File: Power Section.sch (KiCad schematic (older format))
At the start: 21 parts, among them J1 BATT, J17 CK-JS102011SAQN, Q1 IRLML9301TRPBF, Q7 IRLML9301TRPBF, U1 LM1117LDX, U2 LM1117LDX

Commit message: Holy $hi3t
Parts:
- added J10, J5, J9: BATT, Connector_PinHeader_2.54mm:PinHeader_1x02_P2.54mm_Vertical, symbol Connector_Generic:Conn_01x02
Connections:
- net BATT+: now also J9.1 (Pin_1)
- net GND: now also J10.2 (Pin_2), J5.2 (Pin_2); no longer J1.2 (Pin_2)
- new net: J1.2 (Pin_2), J10.1 (Pin_1), J5.1 (Pin_1), J9.2 (Pin_2)
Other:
- moved on the sheet: J1
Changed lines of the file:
@@
 L Connector_Generic:Conn_01x02 J1
 U 1 1 5E80D37A
-P 1550 2700
-F 0 "J1" H 1468 2917 50  0000 C CNN
-F 1 "BATT" H 1468 2826 50  0000 C CNN
-F 2 "Connector_PinHeader_2.54mm:PinHeader_1x02_P2.54mm_Vertical" H 1550 2700 50  0001 C CNN
-F 3 "~" H 1550 2700 50  0001 C CNN
-	1    1550 2700
+P 1250 2700
+F 0 "J1" H 1168 2917 50  0000 C CNN
+F 1 "BATT" H 1168 2826 50  0000 C CNN
+F 2 "Connector_PinHeader_2.54mm:PinHeader_1x02_P2.54mm_Vertical" H 1250 2700 50  0001 C CNN
+F 3 "~" H 1250 2700 50  0001 C CNN
+	1    1250 2700
 	-1   0    0    -1
 $EndComp
-Wire Wire Line
-	1750 2800 1900 2800
 Wire Wire Line
 	3800 2900 4200 2900
@@
 L power:GND #PWR0195
 U 1 1 5E892532
-P 1900 3550
-F 0 "#PWR0195" H 1900 3300 50  0001 C CNN
-F 1 "GND" H 1905 3377 50  0000 C CNN
-F 2 "" H 1900 3550 50  0001 C CNN
-F 3 "" H 1900 3550 50  0001 C CNN
-	1    1900 3550
+P 1800 3550
+F 0 "#PWR0195" H 1800 3300 50  0001 C CNN
+F 1 "GND" H 1805 3377 50  0000 C CNN
+F 2 "" H 1800 3550 50  0001 C CNN
+F 3 "" H 1800 3550 50  0001 C CNN
+	1    1800 3550
 	1    0    0    -1
 $EndComp
@@
 	1    0    0    1
 $EndComp
-Wire Wire Line
-	2100 2700 1750 2700
 $Comp
 L Device:R_Small R51
@@
 $EndComp
 Wire Wire Line
-	1900 2800 1900 3550
-Wire Wire Line
 	3800 3100 3800 3550
-Connection ~ 1900 3550
+Connection ~ 1800 3550
 Wire Wire Line
 	3050 3400 3050 3550
 Wire Wire Line
 	3050 3550 3550 3550
-Wire Wire Line
-	1900 3550 3050 3550
-Connection ~ 3050 3550
 Wire Wire Line
 	3350 2700 3550 2700
@@
 Text Notes 3550 2500 0    50   ~ 0
 1:3 voltage divider
+$Comp
+L Connector_Generic:Conn_01x02 J5
+U 1 1 5F9516BF
+P 1250 3100
+F 0 "J5" H 1168 3317 50  0000 C CNN
+F 1 "BATT" H 1168 3226 50  0000 C CNN
+F 2 "Connector_PinHeader_2.54mm:PinHeader_1x02_P2.54mm_Vertical" H 1250 3100 50  0001 C CNN
+F 3 "~" H 1250 3100 50  0001 C CNN
+	1    1250 3100
+	-1   0    0    -1
+$EndComp
+$Comp
+L Connector_Generic:Conn_01x02 J9
+U 1 1 5F956258
+P 1600 2700
+F 0 "J9" H 1518 2917 50  0000 C CNN
+F 1 "BATT" H 1518 2826 50  0000 C CNN
+F 2 "Connector_PinHeader_2.54mm:PinHeader_1x02_P2.54mm_Vertical" H 1600 2700 50  0001 C CNN
+F 3 "~" H 1600 2700 50  0001 C CNN
+	1    1600 2700
+	-1   0    0    -1
+$EndComp
+$Comp
+L Connector_Generic:Conn_01x02 J10
+U 1 1 5F95794D
+P 1600 3100
+F 0 "J10" H 1518 3317 50  0000 C CNN
+F 1 "BATT" H 1518 3226 50  0000 C CNN
+F 2 "Connector_PinHeader_2.54mm:PinHeader_1x02_P2.54mm_Vertical" H 1600 3100 50  0001 C CNN
+F 3 "~" H 1600 3100 50  0001 C CNN
+	1    1600 3100
+	-1   0    0    -1
+$EndComp
+Wire Wire Line
+	1450 2700 1800 2700
+Connection ~ 1800 2700
+Wire Wire Line
+	1450 2800 1800 2800
+Wire Wire Line
+	1800 2800 1800 3100
+Connection ~ 1800 2800
+Wire Wire Line
+	1450 3100 1800 3100
+Connection ~ 1800 3100
+Wire Wire Line
+	1450 3200 1800 3200
+Connection ~ 1800 3200
+Wire Wire Line
+	1800 3200 1800 3550
+Wire Wire Line
+	1800 2700 2100 2700
+Wire Wire Line
+	1800 3550 3050 3550
+Connection ~ 3050 3550
 $EndSCHEMATC

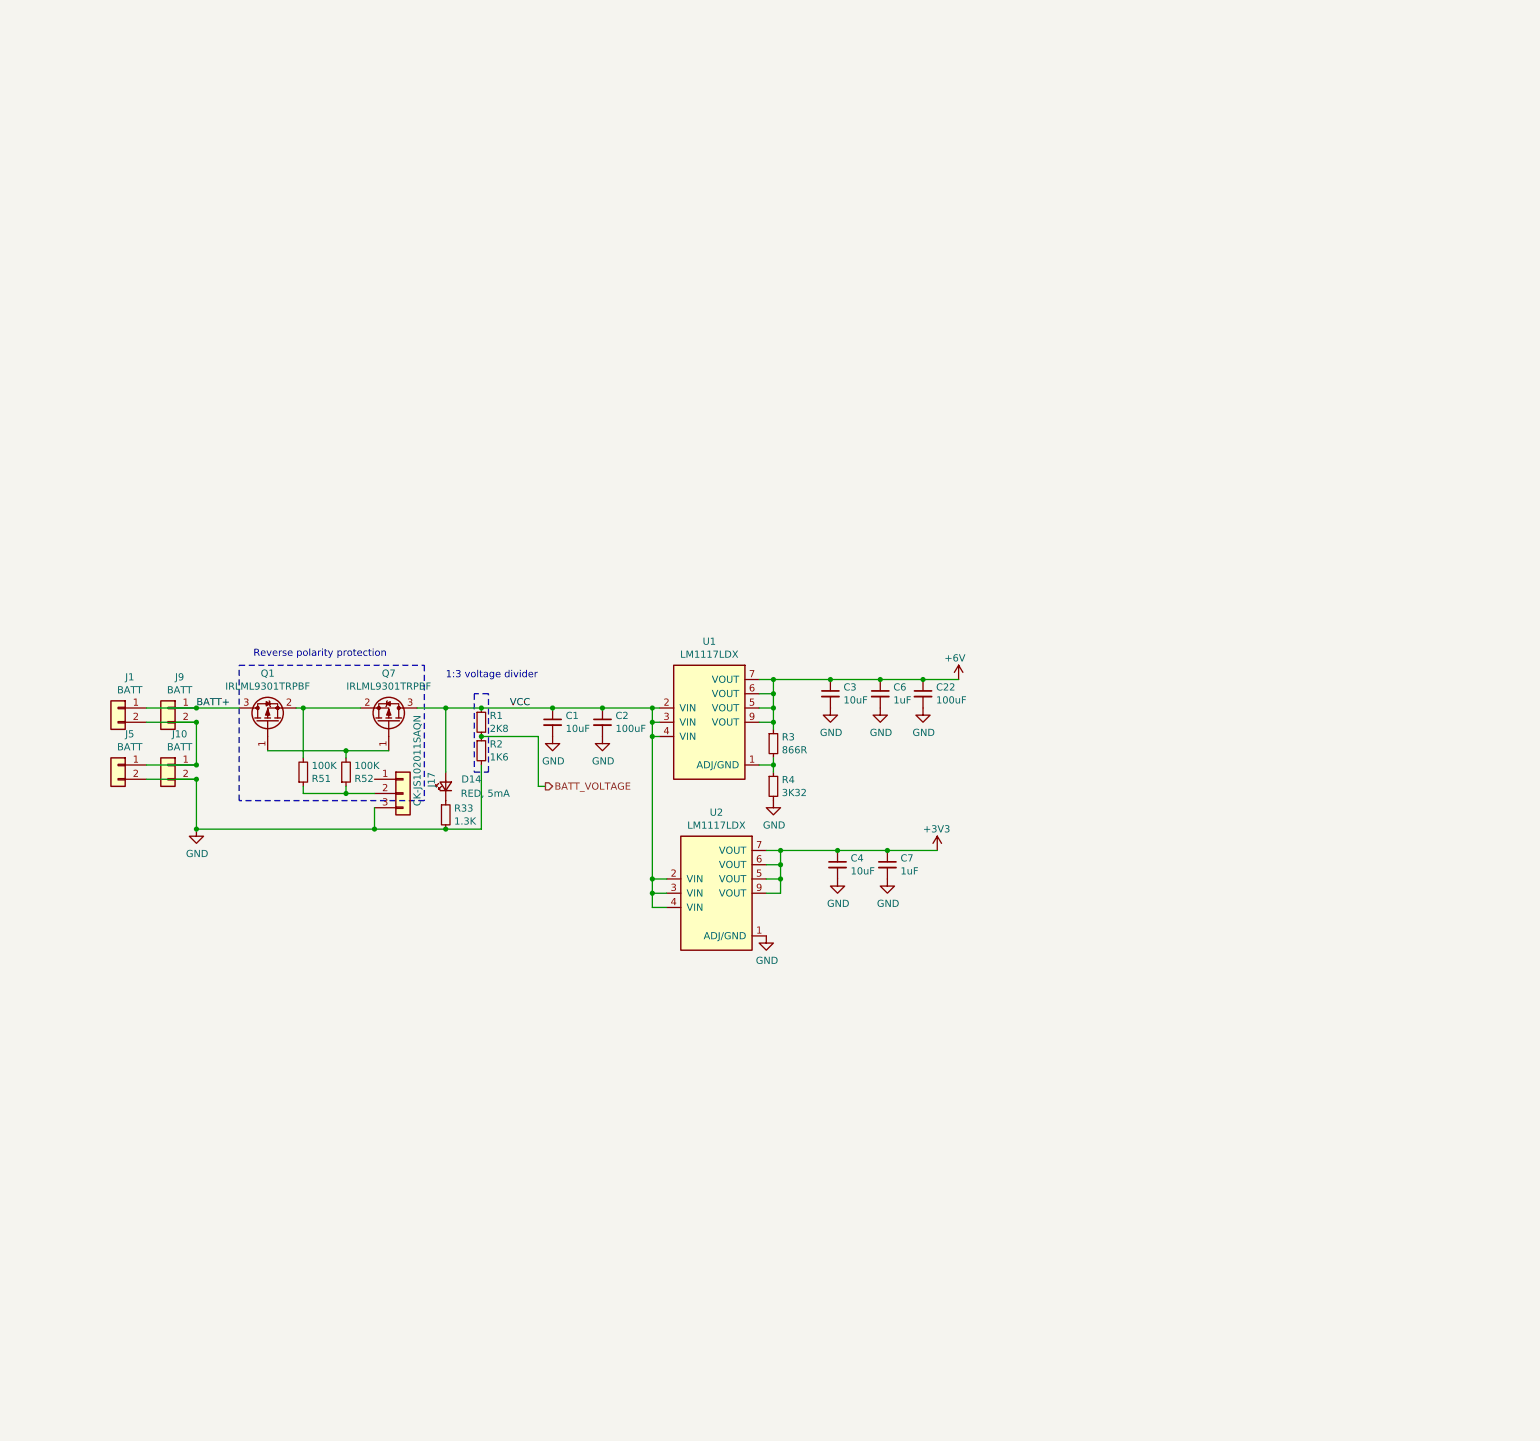
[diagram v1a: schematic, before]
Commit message: USB-C PD charging and cell balancing.
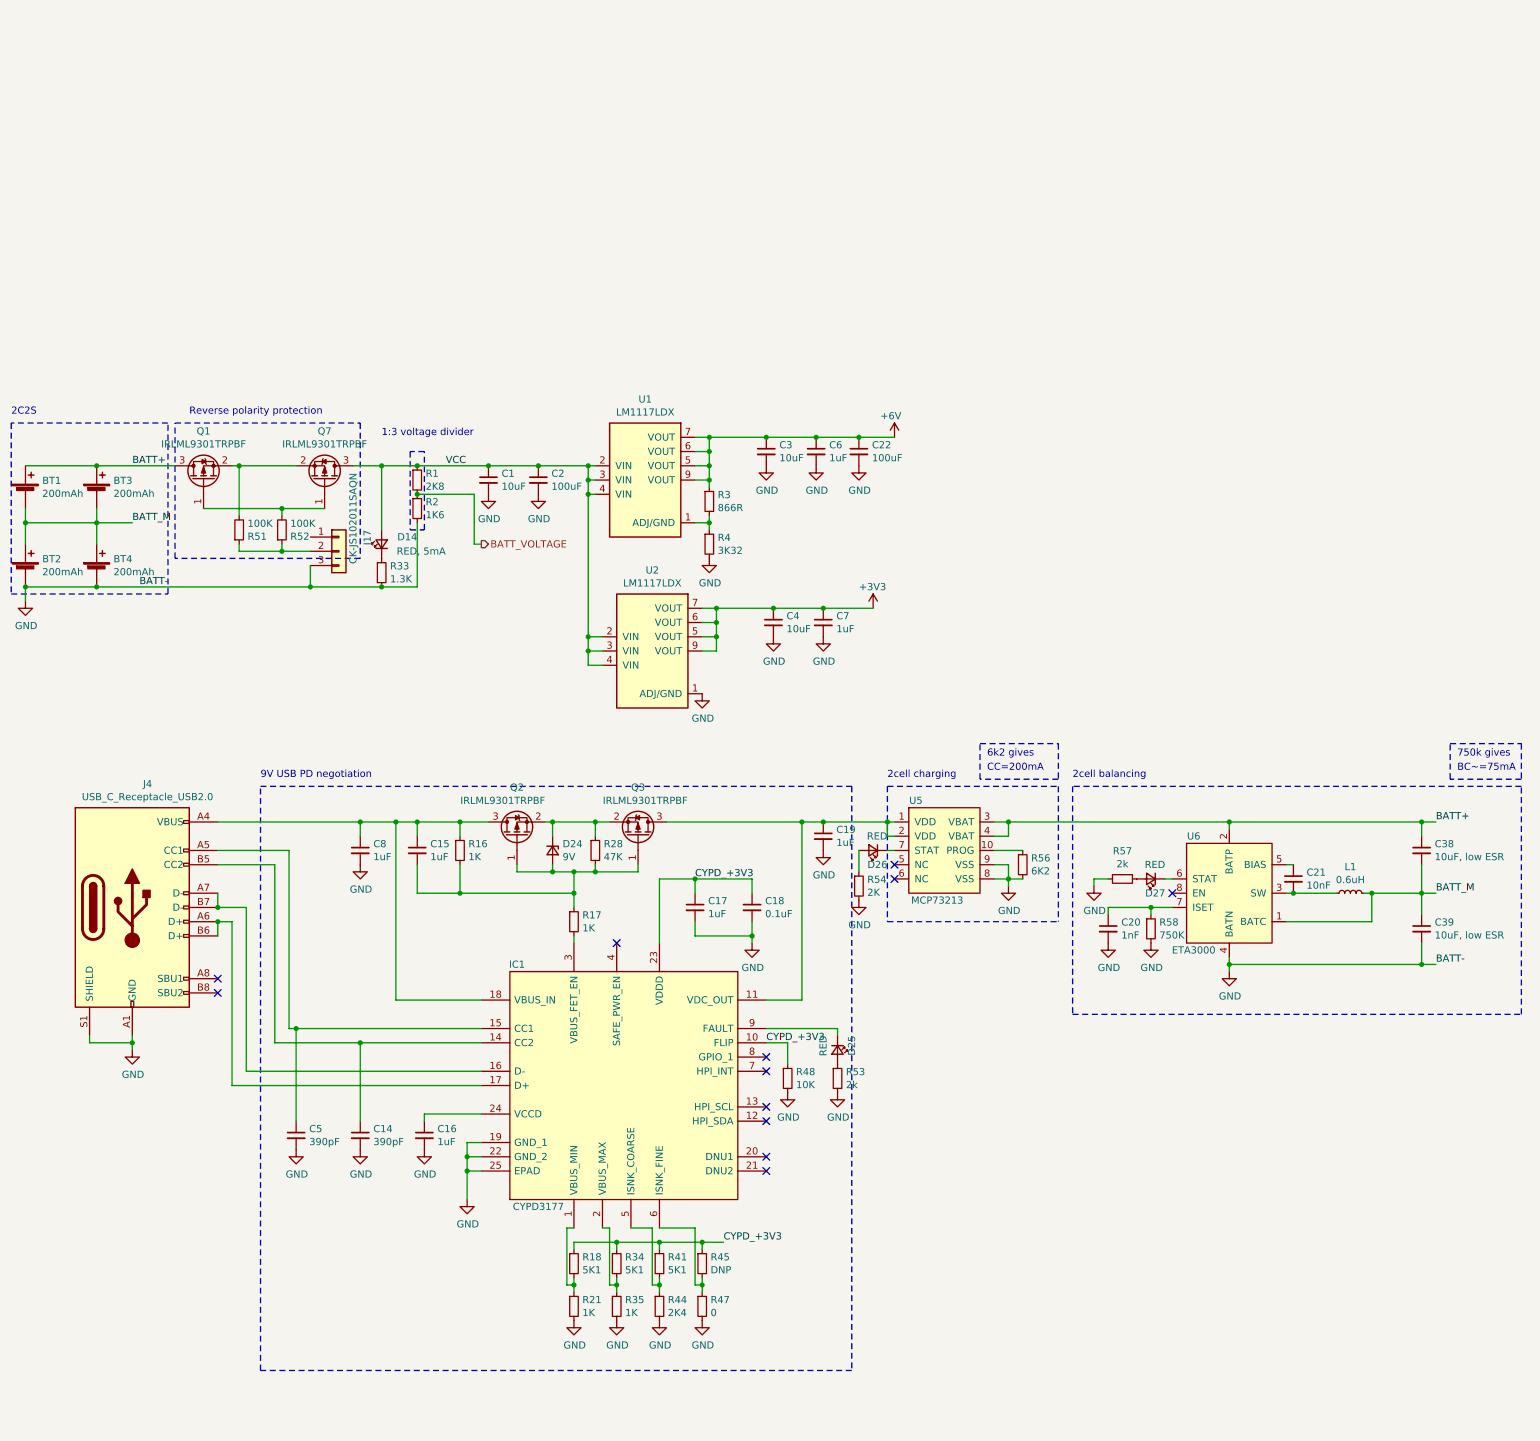
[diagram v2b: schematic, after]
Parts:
- removed J1, J10, J5, J9: BATT, Connector_PinHeader_2.54mm:PinHeader_1x02_P2.54mm_Vertical, symbol Connector_Generic:Conn_01x02
- added BT1, BT2, BT3, BT4: 200mAh, Connector_PinHeader_1.27mm:PinHeader_1x02_P1.27mm_Vertical, symbol Device:Battery_Cell
- added C14, C5: 390pF, Capacitor_SMD:C_0603_1608Metric, symbol Device:C_Small
- added C15, C16, C17, C19, C8: 1uF, Capacitor_SMD:C_0603_1608Metric, symbol Device:C_Small
- added C18: 0.1uF, Capacitor_SMD:C_0603_1608Metric, symbol Device:C_Small
- added C20: 1nF, Capacitor_SMD:C_0603_1608Metric, symbol Device:C_Small
- added C21: 10nF, Capacitor_SMD:C_0603_1608Metric, symbol Device:C_Small
- added C38, C39: 10uF, low ESR, Capacitor_SMD:C_0603_1608Metric, symbol Device:C_Small
- added D24: 9V, Diode_SMD:D_SOD-52, symbol Device:D_Zener_Small
- added D25, D26, D27: RED, LED_SMD:LED_0402_1005Metric, symbol Device:LED_Small
- added IC1: CYPD3177, CYPD3177-24LQXI:QFN50P400X400X60-25N-D, symbol CYPD3177-24LQXI:CYPD3177
- added J4: USB_C_Receptacle_USB2.0, Connector_USB:USB_C_Receptacle_GCT_USB4085, symbol Connector:USB_C_Receptacle_USB2.0
- added L1: 0.6uH, Inductor_SMD:L_0603_1608Metric, symbol Device:L_Small
- added Q2, Q3: IRLML9301TRPBF, Package_TO_SOT_SMD:SOT-23, symbol Device:Q_PMOS_GSD
- added R16, R17, R21, R35: 1K, Resistor_SMD:R_0402_1005Metric, symbol Device:R_Small
- added R18, R34, R41: 5K1, Resistor_SMD:R_0402_1005Metric, symbol Device:R_Small
- added R28: 47K, Resistor_SMD:R_0402_1005Metric, symbol Device:R_Small
- added R44: 2K4, Resistor_SMD:R_0402_1005Metric, symbol Device:R_Small
- added R45: DNP, Resistor_SMD:R_0402_1005Metric, symbol Device:R_Small
- added R47: 0, Resistor_SMD:R_0402_1005Metric, symbol Device:R_Small
- added R48: 10K, Resistor_SMD:R_0402_1005Metric, symbol Device:R_Small
- added R53, R57: 2k, Resistor_SMD:R_0402_1005Metric, symbol Device:R_Small
- added R54: 2K, Resistor_SMD:R_0402_1005Metric, symbol Device:R_Small
- added R56: 6K2, Resistor_SMD:R_0402_1005Metric, symbol Device:R_Small
- added R58: 750K, Resistor_SMD:R_0402_1005Metric, symbol Device:R_Small
- added U5: MCP73213, Package_DFN_QFN:DFN-10-1EP_3x3mm_P0.5mm_EP1.55x2.48mm, symbol synermycha-electronics:MCP73213
- added U6: ETA3000, Package_DFN_QFN:DFN-8-1EP_2x2mm_P0.5mm_EP0.6x1.2mm, symbol synermycha-electronics:ETA3000
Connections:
- net BATT+: now also BT1.1 (+), BT3.1 (+), C38.1, U5.3 (VBAT), U5.4 (VBAT), U6.2 (BATP)
- net GND: now also BT2.2 (-), BT4.2 (-), C14.2, C16.2, C17.2, C18.2, C19.2, C20.2, C39.2, C5.2, C8.2, IC1.19 (GND_1), IC1.22 (GND_2), IC1.25 (EPAD), J4.A1 (GND), J4.A12 (GND), J4.B1 (GND), J4.B12 (GND), J4.S1 (SHIELD), R21.2, R35.2, R44.2, R47.2, R48.2, R53.2, R54.2, R56.2, R57.2, R58.2, U5.8 (VSS), U5.9 (VSS), U6.4 (BATN)
- new net: IC1.1 (VBUS_MIN), R18.2, R21.1
- new net: C19.1, IC1.11 (VDC_OUT), Q3.3 (D), U5.1 (VDD), U5.2 (VDD)
- new net: C14.1, IC1.14 (CC2), J4.B5 (CC2)
- new net: C5.1, IC1.15 (CC1), J4.A5 (CC1)
- new net: IC1.16 (D-), J4.A7 (D-), J4.B7 (D-)
- new net: IC1.17 (D+), J4.A6 (D+), J4.B6 (D+)
- new net: C15.1, C8.1, IC1.18 (VBUS_IN), J4.A4 (VBUS), J4.A9 (VBUS), J4.B4 (VBUS), J4.B9 (VBUS), Q2.3 (D), R16.1
- new net: IC1.2 (VBUS_MAX), R34.2, R35.1
- new net: C16.1, IC1.24 (VCCD)
- new net: IC1.3 (VBUS_FET_EN), R17.2
- new net: IC1.5 (ISNK_COARSE), R41.2, R44.1
- new net: IC1.6 (ISNK_FINE), R45.2, R47.1
- new net: D25.1 (K), IC1.9 (FAULT)
- new net: C21.2, L1.1, U6.3 (SW)
- new net: C21.1, U6.5 (BIAS)
- new net: D27.1 (K), U6.6 (STAT)
- new net: C20.1, R58.1, U6.7 (ISET)
- new net: R56.1, U5.10 (PROG)
- new net: D26.1 (K), U5.7 (STAT)
- new net: C15.2, D24.2 (A), Q2.1 (G), Q3.1 (G), R16.2, R17.1, R28.2
- new net: D24.1 (K), Q2.2 (S), Q3.2 (S), R28.1
- new net: D27.2 (A), R57.1
- new net: D25.2 (A), R53.1
- new net: D26.2 (A), R54.1
- new net BATT_M: BT1.2 (-), BT2.1 (+), BT3.2 (-), BT4.1 (+), C38.2, C39.1, L1.2, U6.1 (BATC)
- new net CYPD_+3V3: C17.1, C18.1, IC1.10 (FLIP), IC1.23 (VDDD), R18.1, R34.1, R41.1, R45.1, R48.1
- no-connect marks 0 -> 12
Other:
- note added: "2C2S"
- note added: "2cell balancing"
- note added: "2cell charging"
- note added: "6k2 gives"
- note added: "750k gives"
- note added: "9V USB PD negotiation"
- note added: "BC~~=75mA"
- note added: "CC=200mA"
- moved on the sheet: C1, C2, C22, C3, C4, C6, C7, D14, J17, Q1, Q7, R1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
